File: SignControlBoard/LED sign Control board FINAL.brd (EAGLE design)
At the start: 70.8 x 59.7 mm, 48 parts, among them IC1 MSGEQ7DIL, U1 ATMEGA328P, U2 M5205 5v, Y1 16MHz

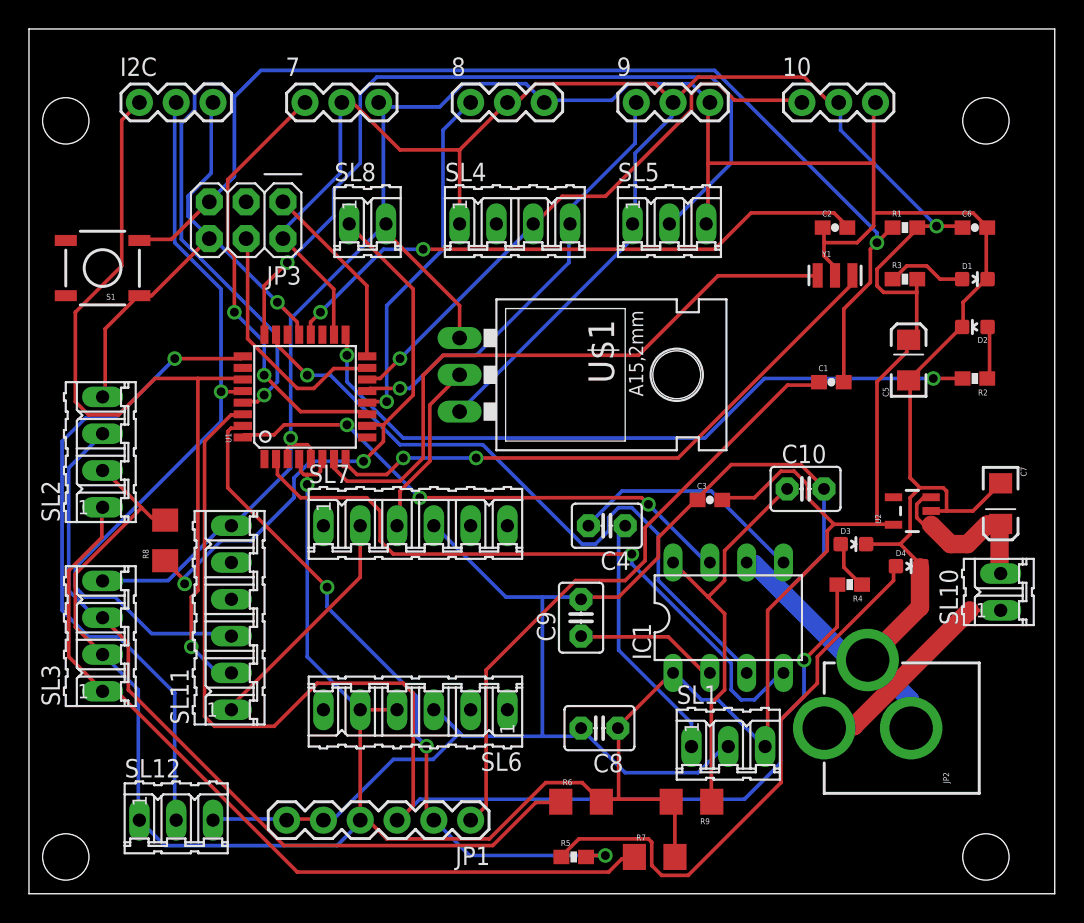
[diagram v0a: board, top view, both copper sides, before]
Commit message: Updated control and sign boards. Removed old versions
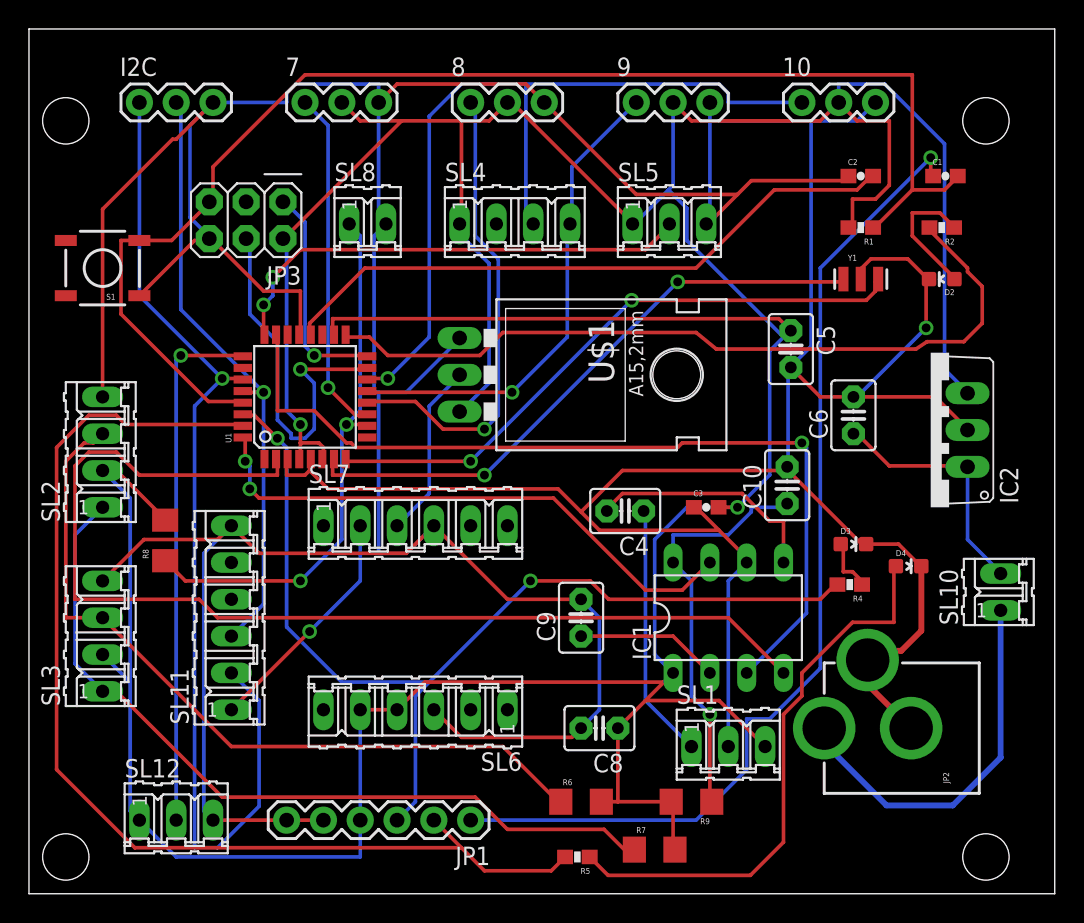
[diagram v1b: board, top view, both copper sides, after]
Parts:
- removed C7: 10uF, SparkFun-Passives:EIA3216
- removed D1: Power, SparkFun-LED:LED-0603
- removed R3: 10k, SparkFun-Passives:0603-RES
- removed U2: M5205 5v, SparkFun-PowerIC:SOT23-5
- added IC2: 7805TV, linear:TO220V
- C5: value 10uF -> 0.1uf; device SparkFun-Passives:EIA3216 -> capacitor-wima:C2.5-3
- C6: value 0.1uF -> 0.33uf; device SparkFun-Passives:0603-CAP -> capacitor-wima:C2.5-3
- moved C1 16.3 mm to (63.2, 48.3)
- moved C6 15.4 mm to (56.9, 31.8), turned to 90 degrees
- moved R2 10.7 mm to (63.0, 44.7)
- moved C5 8.16 mm to (52.6, 36.3), turned to 270 degrees
- moved D2 4.02 mm to (63.0, 41.1)
- moved C2 3.98 mm to (57.4, 48.3)
- moved R1 3.05 mm to (57.4, 44.7), turned to 180 degrees
- moved Y1 1.80 mm to (57.4, 41.1)
- moved C4 1.63 mm to (41.1, 25.1)
- moved C10 1.30 mm to (52.3, 26.9), turned to 90 degrees
- moved C3 0.57 mm to (46.7, 25.4)
- moved R7 0.51 mm to (43.2, 1.78)
- moved R5 0.25 mm to (37.8, 1.27), turned to 180 degrees
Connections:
- removed net N$3: D1.A, R3.1
- net GND: now also C5.2, IC2.2; no longer C5.C, C7.C, D1.C, U2.2
- net VCC: now also C5.1, IC2.3; no longer C5.A, C6.1, R3.2, U2.5
- net VIN: now also C6.1, IC2.1; no longer C7.A, U2.1, U2.3
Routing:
- net GND: track 323.4 -> 407.6 mm, vias 2 -> 1
- net VCC: track 290.3 -> 329.9 mm
- net D4: track 45.9 -> 76.4 mm, vias 1 -> 0
- net TXO: track 48.1 -> 77.4 mm, vias 3 -> 0
- net DTR: track 43.4 -> 70.4 mm, vias 0 -> 1
- net A1: track 56.6 -> 33.2 mm, vias 1 -> 2
- net RXI: track 89.9 -> 70.2 mm, vias 1 -> 2
- net D10: track 39.7 -> 58.1 mm
- net SDA: track 57.8 -> 71.7 mm
- net RESET: track 105.8 -> 92.0 mm, vias 2 -> 0
- net A0: track 47.2 -> 60.4 mm
- net SCL: track 52.8 -> 41.7 mm
- net N$8: track 15.5 -> 26.5 mm
- net A2: track 45.5 -> 36.5 mm
- net MOSI: track 17.2 -> 26.1 mm, vias 0 -> 1
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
